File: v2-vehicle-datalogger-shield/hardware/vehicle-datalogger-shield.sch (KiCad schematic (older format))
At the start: 14 parts, among them J1 CONN-SD-CARD-PUSH-PULL-R/A-SMD, J2 FONA808-GPS, J3 OBDII-UART, U1 HOLE, U2 HOLE, U3 HOLE, U4 HOLE, U5 ARDUINO-101-SHIELD

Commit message: Nearly done. Just need to add CC3000 and verify connections.
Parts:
- removed J3: OBDII-UART, Wickerlib:Pin_Header_Straight_1x06, symbol HEADER-FEMALE-6POS-TH-1x06-P0.1IN
- added C?: 1uF, 0805, symbol CAP-CER-1UF-25V-X7R-0805
- added C?: 100nF, 0603, symbol CAP-CER-0.1UF-100V-X7R-0603
- added D?: MBRA140-**, DO214AC, symbol DIODE-SCHOTTKY-20V-1A-DO214AC
- added J?: DB9 TO ENGINE CONTROL UNIT, DB9-FEMALE, symbol HEADER-FEMALE-DB9-SERIAL-TH-9PIN
- added LED?: RED, 0603, symbol LED-RED-0603-SMT-150060RS75000
- added Q?: BSS138, SOT23-3, symbol MOSFET-N-50V-220MA-BSS138
- added R?: 1K, 0402, symbol RES-1K-1%-1/10W-0402
- added R?: 240, 0402, symbol RES-240-1%-1/10W-0402
- added R?: 866, 0402, symbol RES-866-1%-1/10W-0402
- added R?: 374, 0402, symbol RES-374-1%-1/10W-0402
- added U?: LM317MDT, DPAK, symbol IC-VOLT-REG-LDO-ADJ-0.5A-DPAK
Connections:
- net labels added: CAN_HI, CAN_LO, J1850BUS+, J1850BUS-, K-LINE, L-LINE, OBD2_PWM/~VPN, VBAT, VIN
- wire segments 64 -> 91
- no-connect marks 11 -> 7
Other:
- note added: "100V"
- note added: "Adjustable 5.76V or 7.71V"
- note added: "Create a CC3000 breakout for WiFi.\nA0 = IRQ\nD4 = VBEN\nA1 = CS\nD11 = MOSI\nD12 = MISO\nD13 = SCLK\n"
- note added: "Officially 12V, but very noisy.\nCould be up to 14V or higher\nwith higher input spikes."
- note added: "REGULATED\nOUTPUT FROM \nARDUINO 101"
- note added: "microSD Card for logging data.\n\nNeeds to support R/W for data access."
- note removed: "ADAFRUIT FONA808 GSM+GPS MODULE\n\n- 5V shows whether a microUSB is plugged in.\n 5V is there to charge the LiPo; we can leave it plugged in.\n The LiPo must be on-board the FONA808 during use.\n\n- Vbat connects to the LiPo but we don't \n need it on the Arduino so it's unconnected.\n\n- Vio is the logic voltage (3-5V), applied from Arduino 101.\n\n- KEY is on/off and must be pulled low for 2 se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"
- note removed: "OBDII-UART ADAPTER BOARD\n\nThis version of the breakout shield\nneeds external power provided, \nprobably from a 9V battery. \n\nIt is not powered from the OBD-II port.\n\nSerial uses Software UART"
- note removed: "Standard SD Card Interface for logging data.\n\nNeeds to support R/W for data access."
- moved on the sheet: J1, J2, U5A, U5B, U5C, U5D, W1, W2, W3, W4, W5, W6

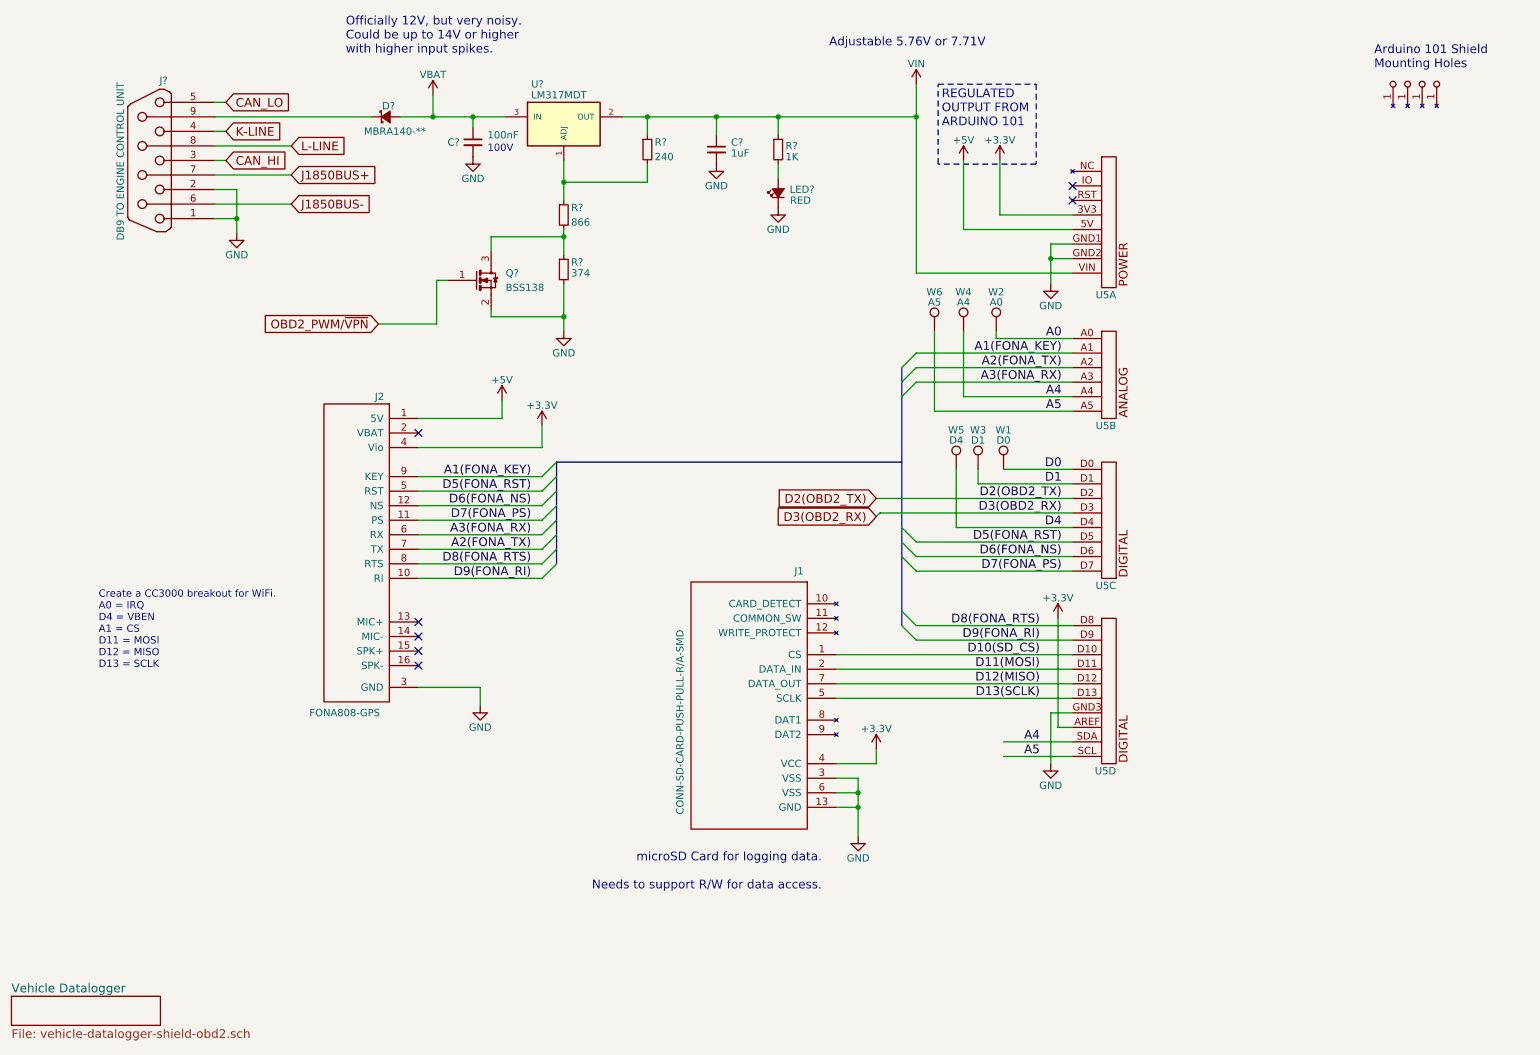
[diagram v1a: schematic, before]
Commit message: Added CC3000 and fixed all other packages. Ready for check.
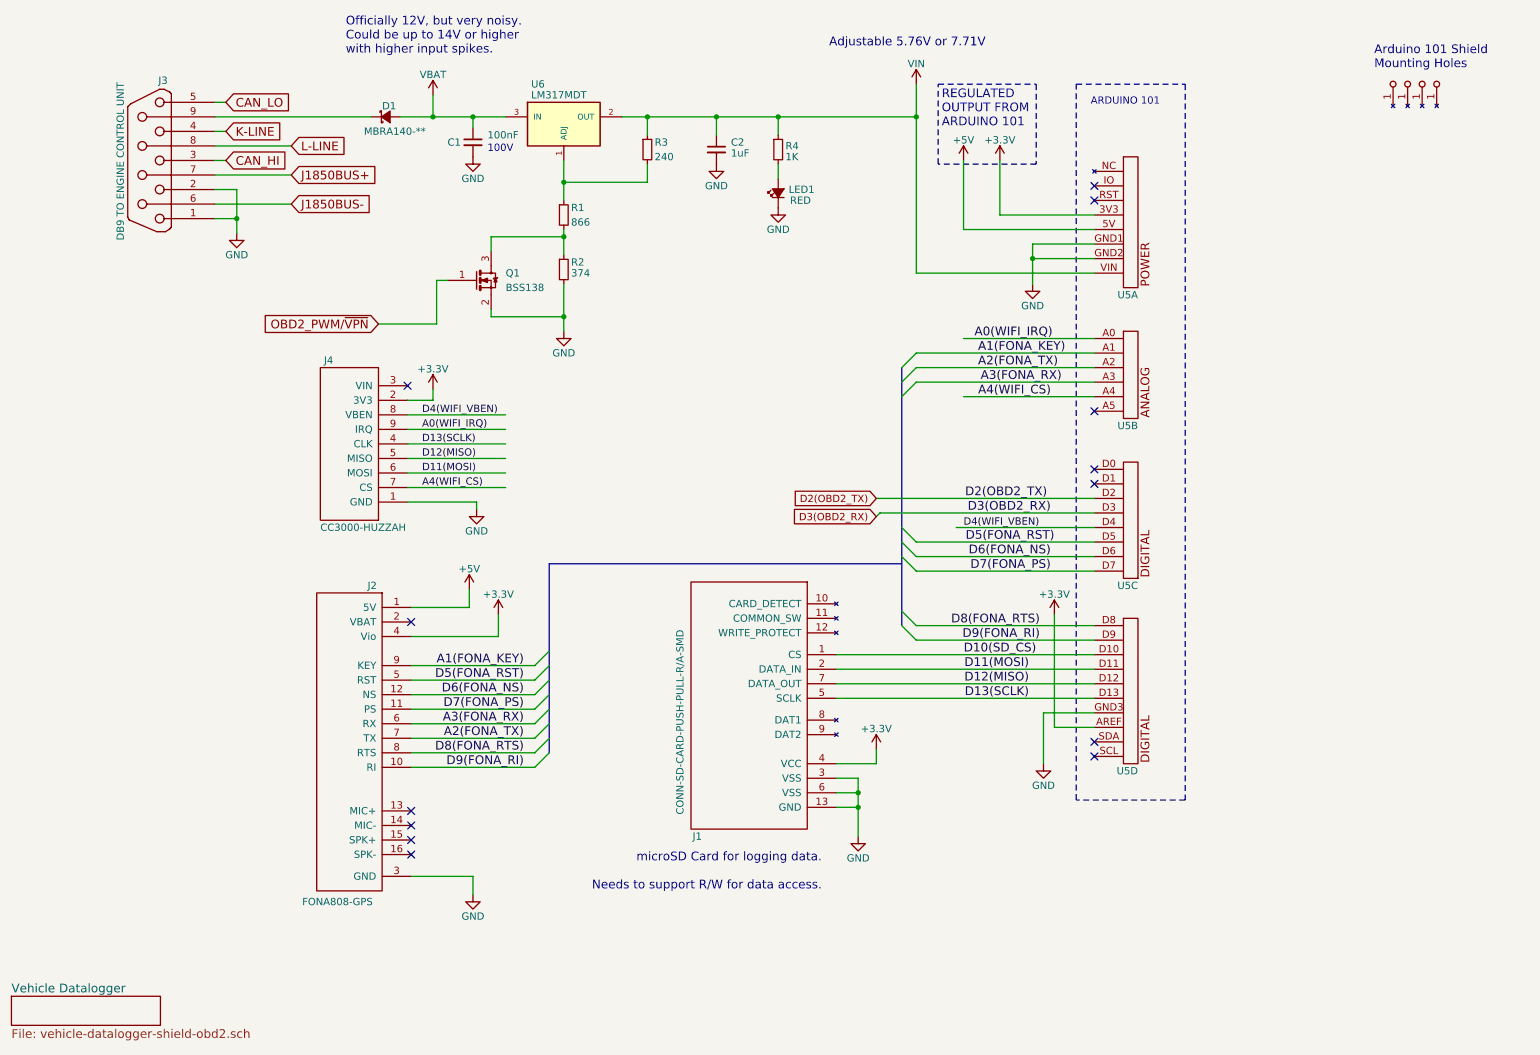
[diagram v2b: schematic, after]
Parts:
- removed W1: D0, Wickerlib:TestHole_1x01, symbol TEST_1P
- removed W2: A0, Wickerlib:TestHole_1x01, symbol TEST_1P
- removed W3: D1, Wickerlib:TestHole_1x01, symbol TEST_1P
- removed W4: A4, Wickerlib:TestHole_1x01, symbol TEST_1P
- removed W5: D4, Wickerlib:TestHole_1x01, symbol TEST_1P
- removed W6: A5, Wickerlib:TestHole_1x01, symbol TEST_1P
- added J4: CC3000-HUZZAH, CC3000-BKOUT, symbol ADAFRUIT-CC3000-WIFI-BREAKOUT
- gave numbers to parts that had none: 11
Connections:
- net labels added: A0(WIFI_IRQ), A4(WIFI_CS), D4(WIFI_VBEN)
- net labels removed: A0, A4, A5, D0, D1, D4
- no-connect marks 7 -> 13
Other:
- note added: "ARDUINO 101"
- note removed: "Create a CC3000 breakout for WiFi.\nA0 = IRQ\nD4 = VBEN\nA1 = CS\nD11 = MOSI\nD12 = MISO\nD13 = SCLK\n"
- moved on the sheet: J2, U5A, U5B, U5C, U5D

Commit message: Pothole vehicle datalogger shield v1.0 schematic is done.
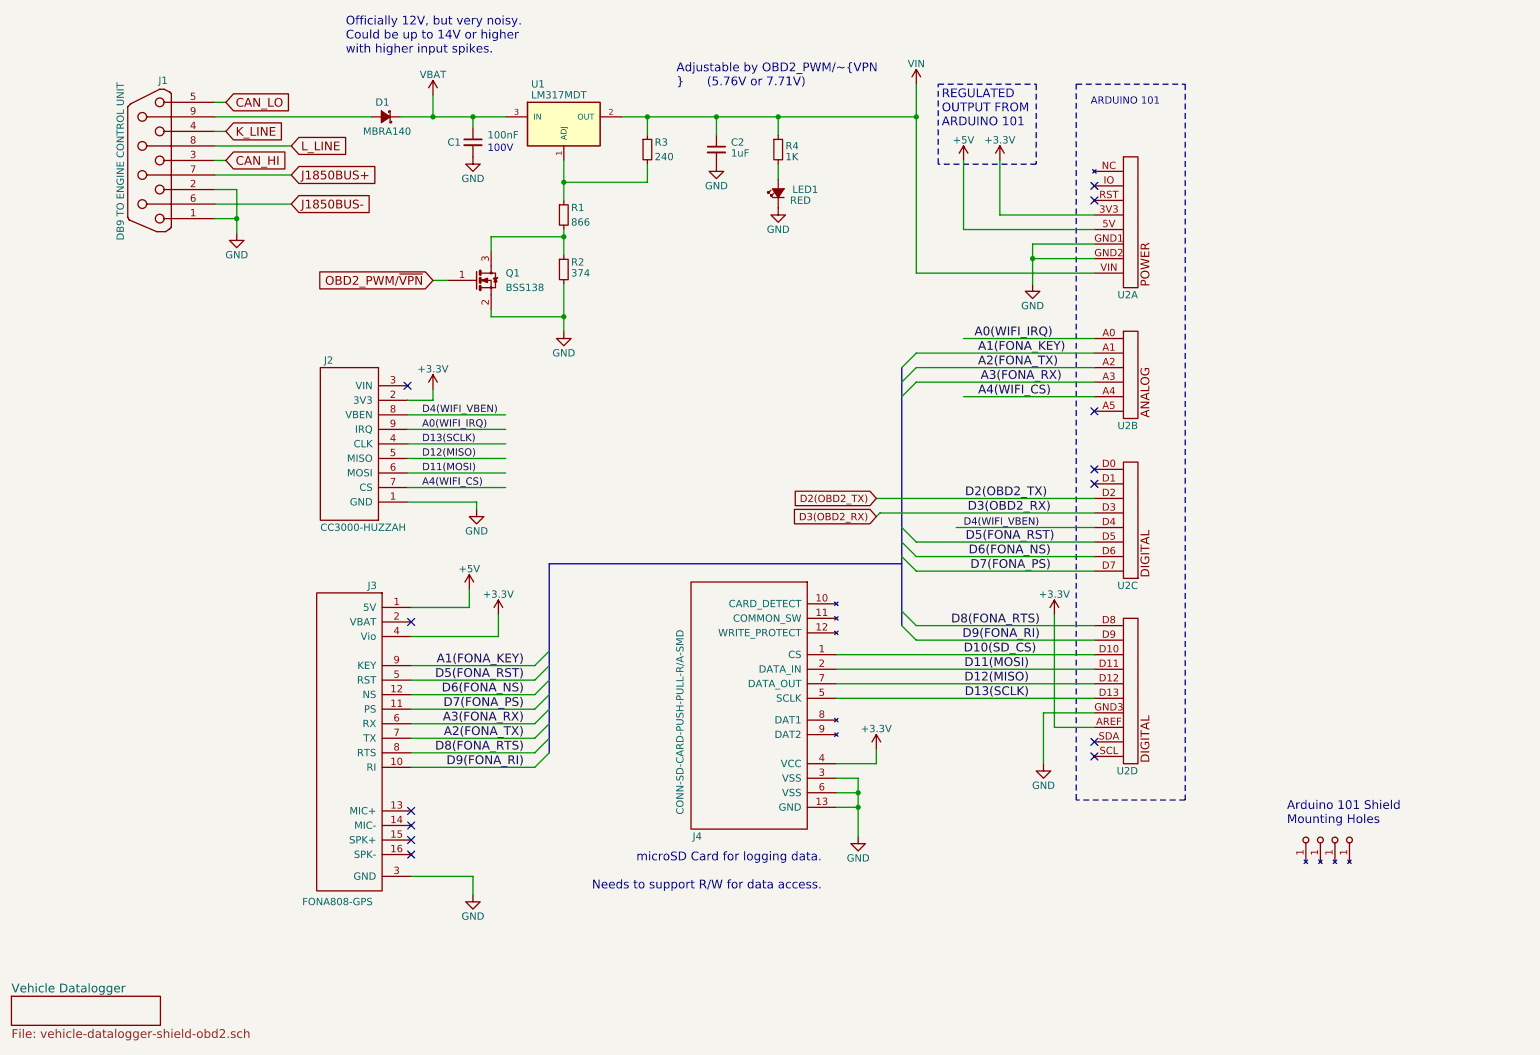
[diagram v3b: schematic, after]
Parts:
- removed D1: MBRA140-**, DO214AC, symbol DIODE-SCHOTTKY-20V-1A-DO214AC
- removed LED1: RED, 0603, symbol LED-RED-0603-SMT-150060RS75000
- added D1: MBRA140, Wickerlib:SMA_Standard, symbol DIODE-SCHOTTKY-40V-1A-MBRA140-SMA
- added LED1: RED, Wickerlib:0603, symbol LED-RED-0603-SMT-HSMS-C191
- C1: footprint 0603 -> Wickerlib:0603
- C2: footprint 0805 -> Wickerlib:0805
- J1: renamed from J3; footprint DB9-FEMALE -> Wickerlib:DB9FC
- Q1: footprint SOT23-3 -> Wickerlib:SOT-23-3
- R1, R2, R3, R4: footprint 0402 -> Wickerlib:0402
- U1: renamed from U6; footprint DPAK -> Wickerlib:DPAK
- renumbered J4 to J2, J2 to J3, J1 to J4, U5 to U2, U1 to U3, U2 to U4, U3 to U5, U4 to U6
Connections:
- net labels added: K_LINE, L_LINE
- net labels removed: K-LINE, L-LINE
- wire segments 91 -> 89
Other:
- note added: "Adjustable by OBD2_PWM/~VPN\n (5.76V or 7.71V)"
- note removed: "Adjustable 5.76V or 7.71V"

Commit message: Added missing footprints, finished symbol-footprint association.
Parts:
- J2: footprint CC3000-BKOUT -> Wickerlib:CC3000BKOUT
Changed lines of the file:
@@
 F 0 "J2" H 2775 4100 50  0000 L CNN
 F 1 "CC3000-HUZZAH" H 2750 2950 50  0000 L CNN
-F 2 "CC3000-BKOUT" H 3075 4775 50  0001 C CIN
+F 2 "Wickerlib:CC3000BKOUT" H 3075 4775 50  0001 C CIN
 F 3 "https://www.adafruit.com/products/1469" H 2950 3550 5   0001 C CNN
 F 4 "CC3000-BKOUT" H 3075 4775 50  0001 C CIN "Package"

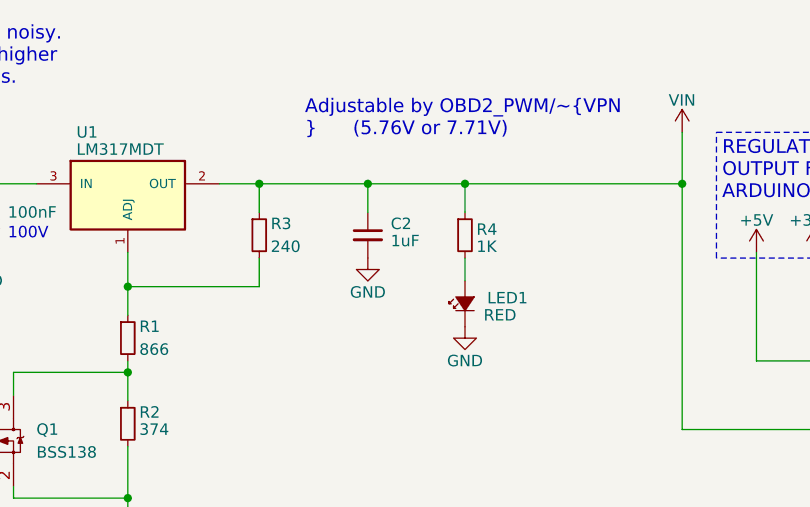
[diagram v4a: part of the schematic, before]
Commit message: Updated schematic, BOM, and spread out footprints. Ready to layout.
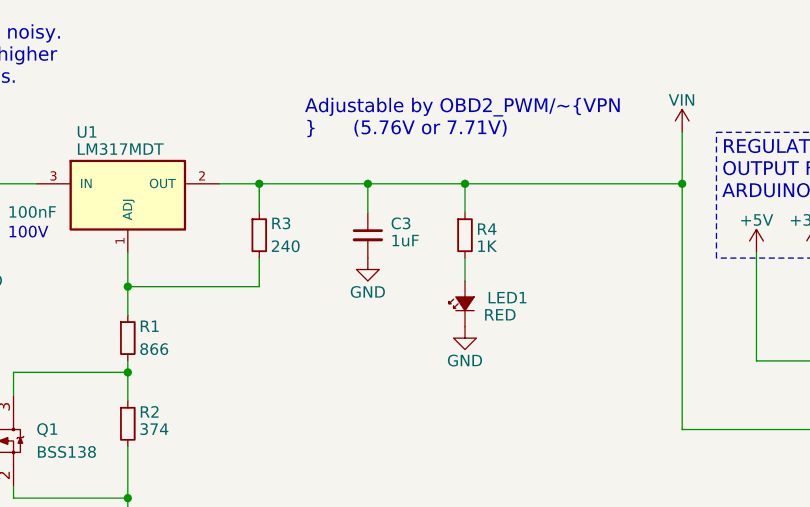
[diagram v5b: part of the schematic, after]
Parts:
- D1: footprint Wickerlib:SMA_Standard -> Wickerlib:Diode_SMA
- renumbered C2 to C3
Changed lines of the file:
@@
 $EndComp
 $Comp
-L CAP-CER-1UF-25V-X7R-0805 C2
+L CAP-CER-1UF-25V-X7R-0805 C3
 U 1 1 57295FB5
 P 5475 1550
-F 0 "C2" H 5575 1600 50  0000 L CNN
+F 0 "C3" H 5575 1600 50  0000 L CNN
 F 1 "1uF" H 5575 1525 50  0000 L CNN
 F 2 "Wickerlib:0805" H 5475 1200 50  0001 C CIN
@@
 F 0 "D1" H 3175 1225 50  0000 L CNN
 F 1 "MBRA140" H 3025 1425 50  0000 L CNN
-F 2 "Wickerlib:SMA_Standard" H 3200 975 50  0001 C CIN
+F 2 "Wickerlib:Diode_SMA" H 3200 975 50  0001 C CIN
 F 3 "http://www.vishay.com/docs/94301/vs-mbra140trpbf.pdf" H 3200 1325 5   0001 C CNN
 F 4 "SMA_Standard" H 3200 975 50  0001 C CIN "Package"
